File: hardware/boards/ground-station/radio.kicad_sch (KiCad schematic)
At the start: 53 parts, among them J1 U.FL, J3 Conn_Coaxial, J5 U.FL, U1 SX1262IMLTRT, U2 SKY13453-385LF, U201 SW-GPS01, U202 RX5808, Y1 32 MHz

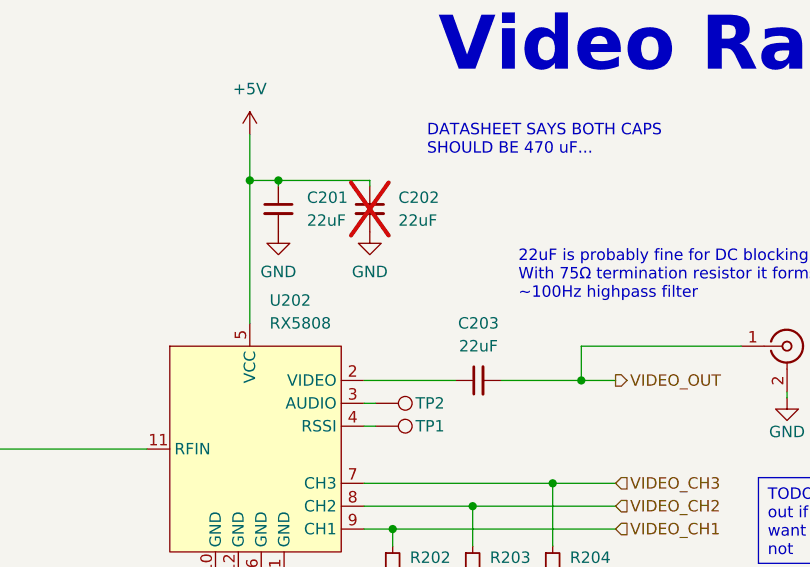
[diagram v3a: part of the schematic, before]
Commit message: Added footprints for most things
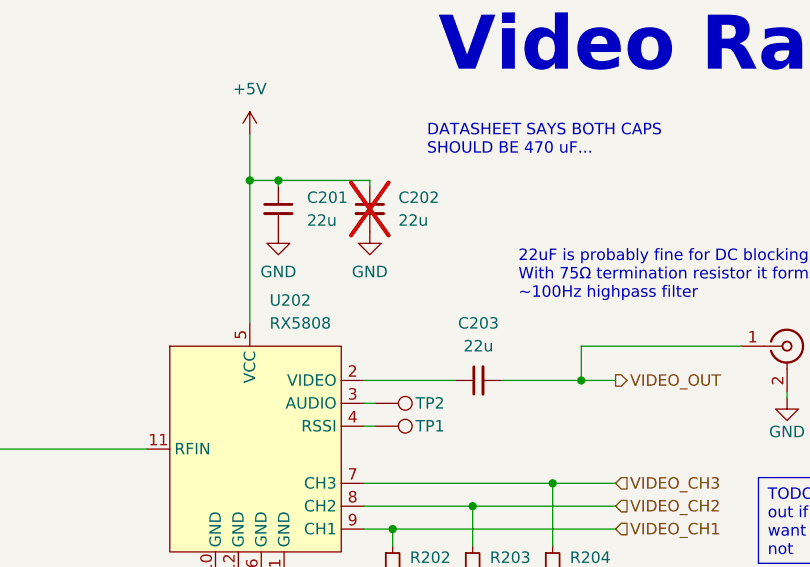
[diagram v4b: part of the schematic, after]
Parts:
- C201, C202, C203: value 22uF -> 22u; footprint (none) -> Capacitor_SMD:C_0805_2012Metric
- R202, R203, R204: footprint (none) -> Resistor_SMD:R_0201_0603Metric
- TP1, TP2: footprint (none) -> TestPoint:TestPoint_THTPad_D2.5mm_Drill1.2mm
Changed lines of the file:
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@@
       (effects (font (size 1.27 1.27)) (justify left))
     )
-    (property "Value" "22uF" (at 80.01 147.3263 0)
-      (effects (font (size 1.27 1.27)) (justify left))
-    )
-    (property "Footprint" "" (at 76.835 146.05 0)
+    (property "Value" "22u" (at 80.01 147.3263 0)
+      (effects (font (size 1.27 1.27)) (justify left))
+    )
+    (property "Footprint" "Capacitor_SMD:C_0805_2012Metric" (at 76.835 146.05 0)
       (effects (font (size 1.27 1.27)) hide)
     )
@@
       (effects (font (size 1.27 1.27)) (justify left))
     )
-    (property "Footprint" "" (at 97.155 186.055 0)
+    (property "Footprint" "Resistor_SMD:R_0201_0603Metric" (at 97.155 186.055 0)
       (effects (font (size 1.27 1.27)) hide)
     )
@@
       (effects (font (size 1.27 1.27)) (justify left) hide)
     )
-    (property "Footprint" "" (at 77.47 172.72 0)
+    (property "Footprint" "TestPoint:TestPoint_THTPad_D2.5mm_Drill1.2mm" (at 77.47 172.72 0)
       (effects (font (size 1.27 1.27)) hide)
     )
@@
       (effects (font (size 1.27 1.27)))
     )
-    (property "Value" "22uF" (at 88.9063 161.29 90)
-      (effects (font (size 1.27 1.27)))
-    )
-    (property "Footprint" "" (at 88.9 165.1 0)
+    (property "Value" "22u" (at 88.9063 161.29 90)
+      (effects (font (size 1.27 1.27)))
+    )
+    (property "Footprint" "Capacitor_SMD:C_0805_2012Metric" (at 88.9 165.1 0)
       (effects (font (size 1.27 1.27)) hide)
     )
@@
       (effects (font (size 1.27 1.27)) (justify left) hide)
     )
-    (property "Footprint" "" (at 77.47 175.26 0)
+    (property "Footprint" "TestPoint:TestPoint_THTPad_D2.5mm_Drill1.2mm" (at 77.47 175.26 0)
       (effects (font (size 1.27 1.27)) hide)
     )
@@
       (effects (font (size 1.27 1.27)) (justify left))
     )
-    (property "Value" "22uF" (at 69.85 147.3263 0)
-      (effects (font (size 1.27 1.27)) (justify left))
-    )
-    (property "Footprint" "" (at 66.675 146.05 0)
+    (property "Value" "22u" (at 69.85 147.3263 0)
+      (effects (font (size 1.27 1.27)) (justify left))
+    )
+    (property "Footprint" "Capacitor_SMD:C_0805_2012Metric" (at 66.675 146.05 0)
       (effects (font (size 1.27 1.27)) hide)
     )
@@
       (effects (font (size 1.27 1.27)) (justify left))
     )
-    (property "Footprint" "" (at 88.265 186.055 0)
+    (property "Footprint" "Resistor_SMD:R_0201_0603Metric" (at 88.265 186.055 0)
       (effects (font (size 1.27 1.27)) hide)
     )
@@
       (effects (font (size 1.27 1.27)) (justify left))
     )
-    (property "Footprint" "" (at 79.375 186.055 0)
+    (property "Footprint" "Resistor_SMD:R_0201_0603Metric" (at 79.375 186.055 0)
       (effects (font (size 1.27 1.27)) hide)
     )
@@
       (effects (font (size 1.27 1.27)) hide)
     )
-    (pin "2")
-    (pin "1")
-    (instances
-      (project "ground-station"
+    (pin "1")
+    (pin "2")
+    (instances
+      (project "ground-station"

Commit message: Added a couple more footprints, changed TVS diode to uni-directional
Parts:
- J3: footprint (none) -> capstone:RCJ-054; Part No (none) -> RCJ-054
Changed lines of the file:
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@@
       (effects (font (size 1.27 1.27)) (justify left))
     )
-    (property "Footprint" "" (at 123.19 161.29 0)
+    (property "Footprint" "capstone:RCJ-054" (at 123.19 161.29 0)
       (effects (font (size 1.27 1.27)) hide)
     )
-    (property "Datasheet" " ~" (at 123.19 161.29 0)
+    (property "Datasheet" "https://www.cuidevices.com/product/resource/rcj-05.pdf" (at 123.19 161.29 0)
       (effects (font (size 1.27 1.27)) hide)
     )
+    (property "Part No" "RCJ-054" (at 123.19 161.29 0)
+      (effects (font (size 1.27 1.27)) hide)
+    )

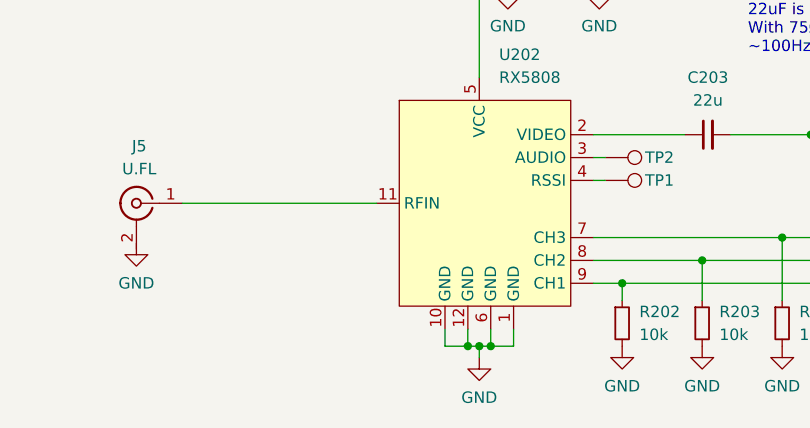
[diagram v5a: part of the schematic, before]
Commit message: Added footprint for RX5808... This footprint should be reviewed
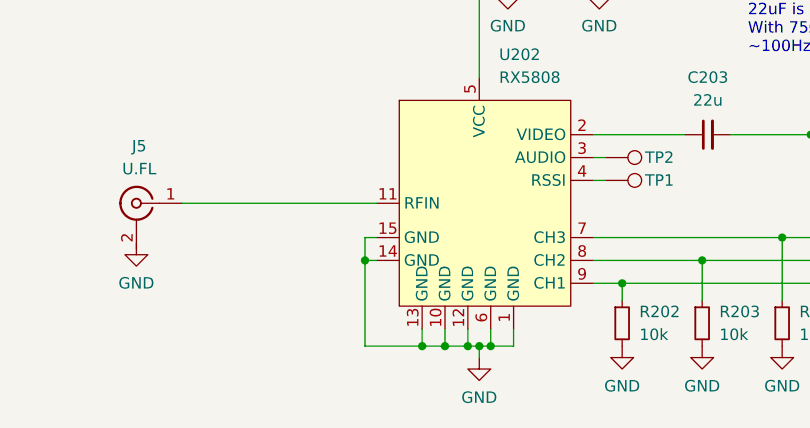
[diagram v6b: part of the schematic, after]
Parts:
- U202: footprint (none) -> capstone:RX5808
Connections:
- net GND: now also U202.13 (GND), U202.14 (GND), U202.15 (GND)

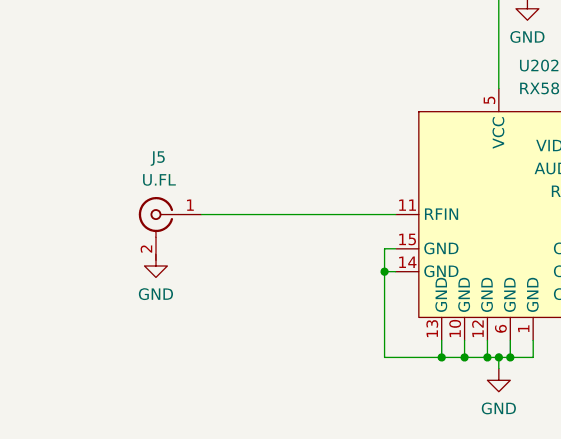
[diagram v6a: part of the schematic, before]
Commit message: Finished initial layout
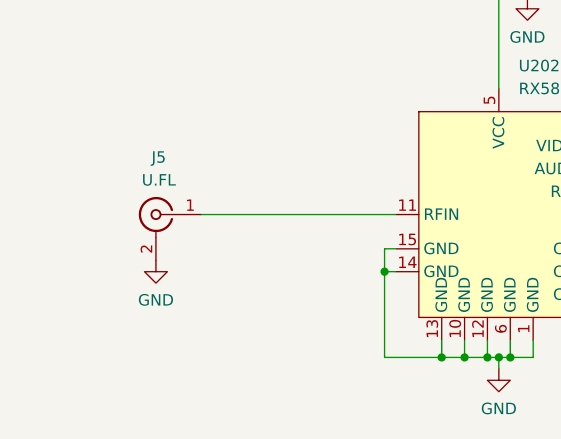
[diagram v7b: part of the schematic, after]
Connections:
- net GND: now also J5.2 (Ext)
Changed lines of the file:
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@@
     )
   )
-  (symbol (lib_id "power:GND") (at 25.4 177.165 0) (unit 1)
+  (symbol (lib_id "power:GND") (at 25.4 177.8 0) (unit 1)
     (in_bom yes) (on_board yes) (dnp no) (fields_autoplaced)
-    (property "Reference" "#PWR0202" (at 25.4 183.515 0)
+    (property "Reference" "#PWR0202" (at 25.4 184.15 0)
       (effects (font (size 1.27 1.27)) hide)
     )
-    (property "Value" "GND" (at 25.4 181.61 0)
+    (property "Value" "GND" (at 25.4 182.245 0)
       (effects (font (size 1.27 1.27)))
     )
-    (property "Footprint" "" (at 25.4 177.165 0)
+    (property "Footprint" "" (at 25.4 177.8 0)
       (effects (font (size 1.27 1.27)) hide)
     )
-    (property "Datasheet" "" (at 25.4 177.165 0)
+    (property "Datasheet" "" (at 25.4 177.8 0)
       (effects (font (size 1.27 1.27)) hide)
     )

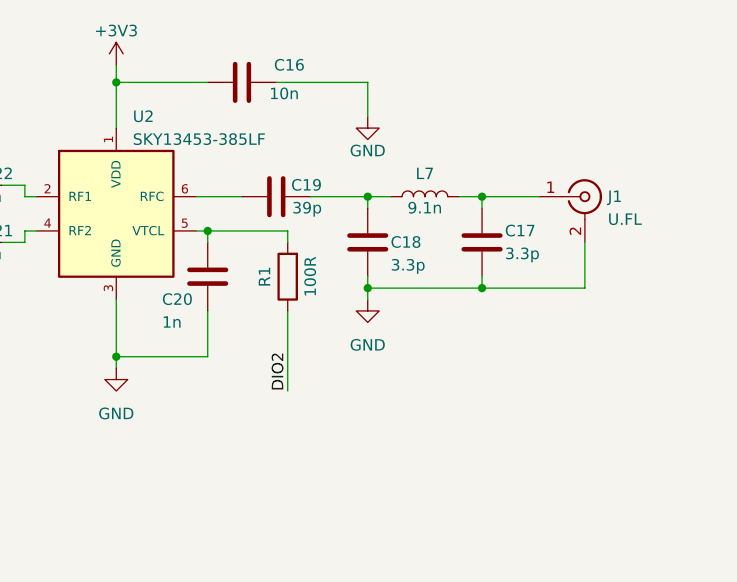
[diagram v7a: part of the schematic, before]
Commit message: Added voltage divider to RF switch VTCL pin to keep voltage to 1.8V. Adjusted cap size to keep RC cutoff frequency consistent
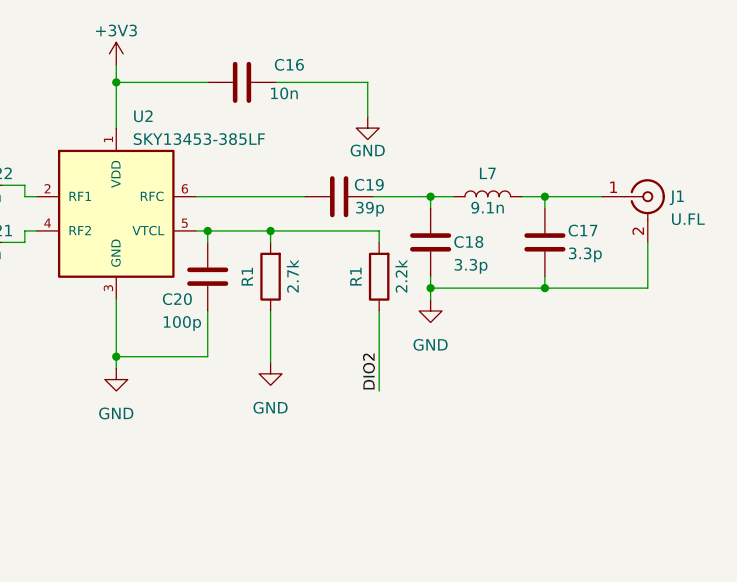
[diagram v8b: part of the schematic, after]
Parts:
- added R1: 2.7k, Resistor_SMD:R_0201_0603Metric, symbol Device:R
- C20: value 1n -> 100p
- R1: value 100R -> 2.2k
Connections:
- net GND: now also R1.1
- net at C20.2, R1.2, U2.5 (VTCL): now also R1.2
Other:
- moved on the sheet: C17, C18, C19, J1, L7, R1
